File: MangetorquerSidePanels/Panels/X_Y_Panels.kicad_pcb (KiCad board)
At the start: 6 copper layers, 82 x 99 mm, 62 parts, among them J6 Through_Hole_1, Q1 BSS138DWQ-7, Q2 MBT2222ADW1T1, Q3 BSS138DWQ-7, Q4 MBT2222ADW1T1, U1 DRV8830DGQ, U2 BD60GC0WEFJ, U3 OPT3001

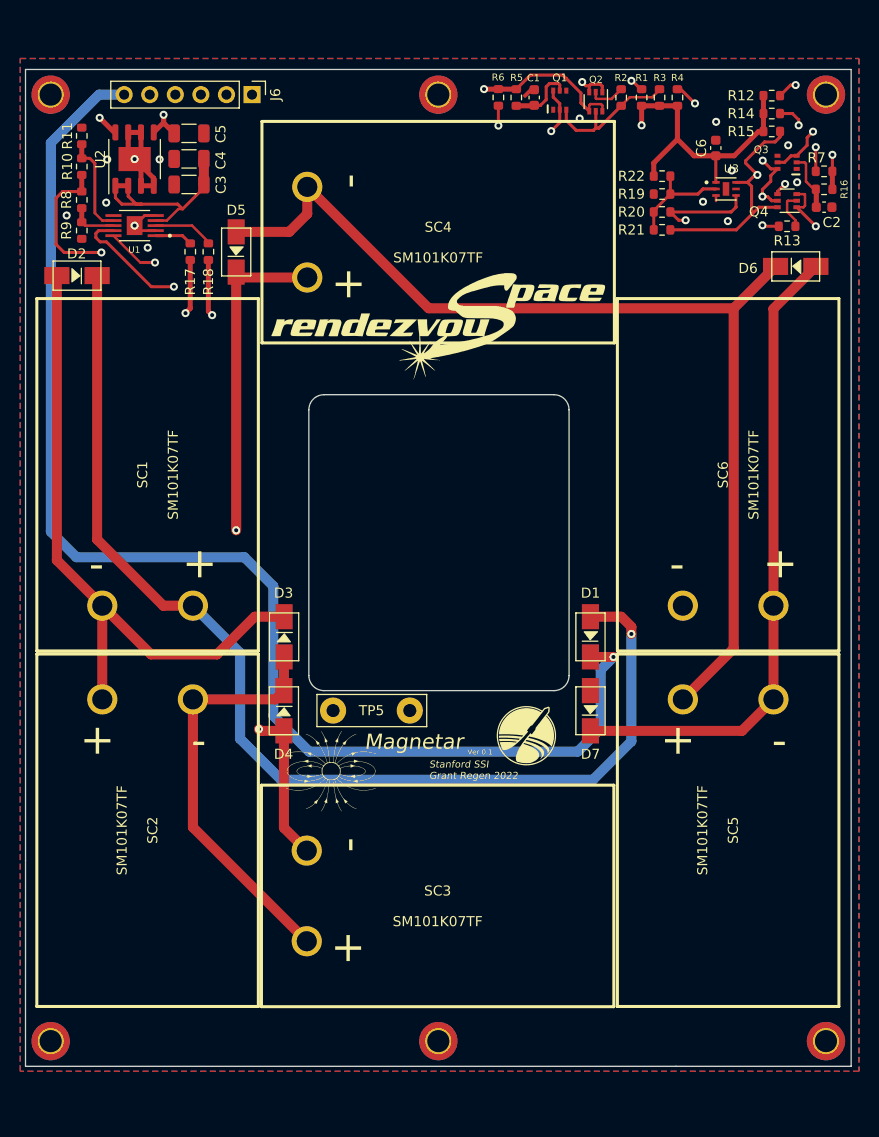
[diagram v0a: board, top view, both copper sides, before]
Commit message: Final flight side panels w/ magnetorquers finished, note final board thickness of 0.031'' and updated copper weight of 0.5oz for internal layers
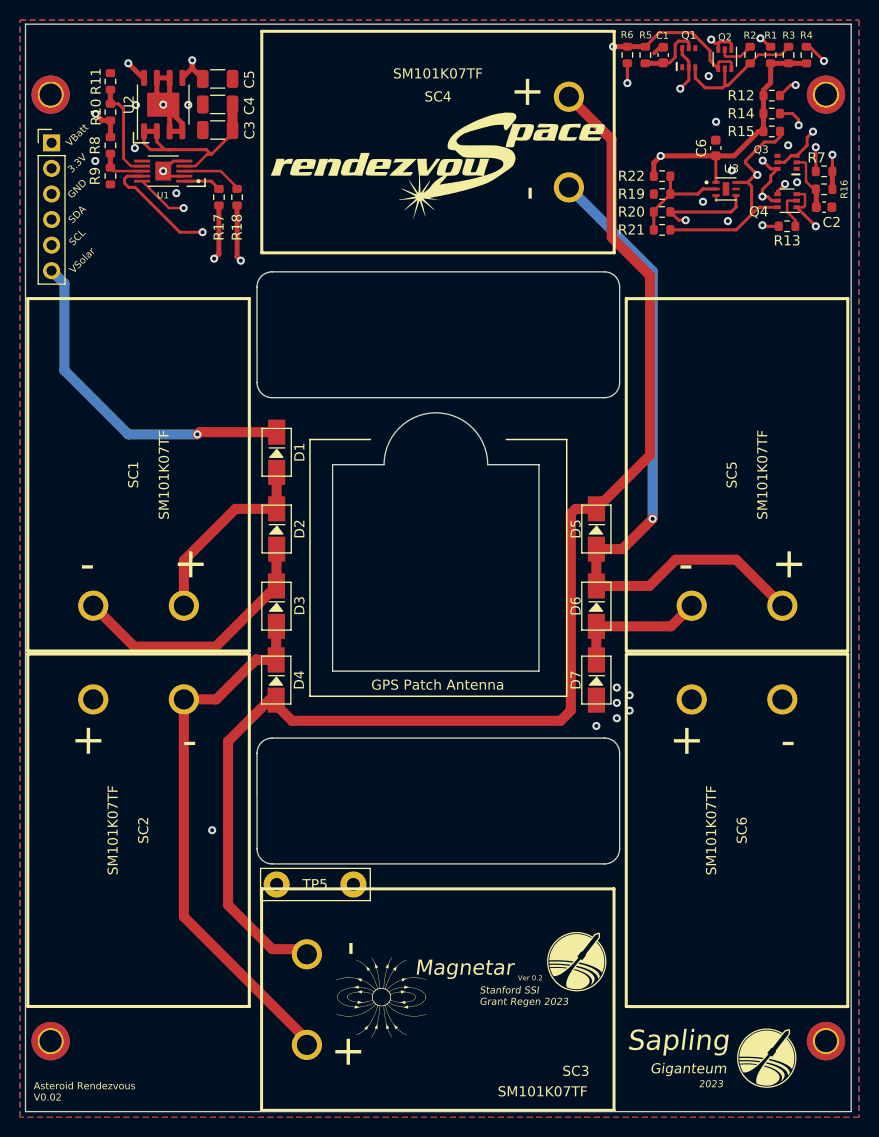
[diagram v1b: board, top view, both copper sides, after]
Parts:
- removed H26, H29: ~, MountingHole:MountingHole_2.2mm_M2_DIN965_Pad_TopBottom
- added REF**: logo_SSI_small, panels:logo_SSI_small, F.Cu at (174.8, 141.0)
- U2: value BD60GC0WEFJ -> BD50GC0WEFJ
- moved D5 45.1 mm to (158.0, 88.1), turned to -90 degrees
- moved D6 39.1 mm to (158.0, 95.8), turned to -90 degrees
- moved D1 36.2 mm to (126.2, 80.5), turned to -90 degrees
- moved SC6 35.3 mm to (172.0, 118.1), turned to 90 degrees
- moved SC5 35.3 mm to (172.0, 82.8), turned to -90 degrees
- moved D2 32.0 mm to (126.2, 88.1), turned to -90 degrees
- moved REF** 23.0 mm to (136.7, 134.6)
- moved REF** 23.0 mm to (155.9, 131.4)
- moved J6 20.5 mm to (103.9, 49.8), turned to 0 degrees
- moved REF** 18.9 mm to (142.7, 49.0)
- moved TP5 18.2 mm to (130.1, 123.9)
- moved REF** 15.9 mm to (142.0, 50.8)
- moved REF** 15.0 mm to (143.9, 132.1)
- moved C1 13.5 mm to (164.6, 41.1)
- moved R2 13.5 mm to (173.3, 41.1)
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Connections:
- R10 pad 1: +3V3 -> VBATT
- R8 pad 1: +3V3 -> VBATT
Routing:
- net VSOLAR: track 129.9 -> 34.2 mm
- net Net-(D1-Pad2): track 111.6 -> 19.5 mm, vias 1 -> 0
- net Net-(D4-Pad2): track 69.0 -> 132.0 mm, vias 2 -> 0
- net Net-(D6-Pad2): track 64.2 -> 23.0 mm
- net Net-(D5-Pad2): track 104.6 -> 68.3 mm, vias 0 -> 1
- net Net-(D2-Pad2): track 65.6 -> 35.4 mm
- net SCL_ISO: track 107.6 -> 137.3 mm
- net SCL: track 54.4 -> 79.4 mm
- net Coil_OUT: track 61.2 -> 85.4 mm, vias 1 -> 2
- net Coil_IN: track 58.5 -> 77.7 mm
- net +3V3: track 107.9 -> 89.9 mm, vias 2 -> 1
- net SDA: track 83.3 -> 96.2 mm
- net Net-(D3-Pad2): track 41.5 -> 53.1 mm
- net VBATT: track 23.6 -> 28.4 mm, vias 2 -> 3
- net SDA_ISO: track 115.5 -> 111.8 mm
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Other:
- board size 82 x 99 mm -> 82 x 108 mm
- board text added: "2023"
- board text added: "3.3V"
- board text added: "Asteroid Rendezvous V0.02"
- board text added: "GND"
- board text added: "GPS Patch Antenna"
- board text added: "Giganteum"
- board text added: "SCL"
- board text added: "SDA"
- board text added: "Sapling"
- board text added: "Stanford SSI Grant Regen 2023"
- board text added: "VBatt"
- board text added: "VSolar"
- board text added: "Ver 0.2"
- board text removed: "Stanford SSI Grant Regen 2022"
- board text removed: "Ver 0.1"
